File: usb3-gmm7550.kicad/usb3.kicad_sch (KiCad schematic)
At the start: 30 parts

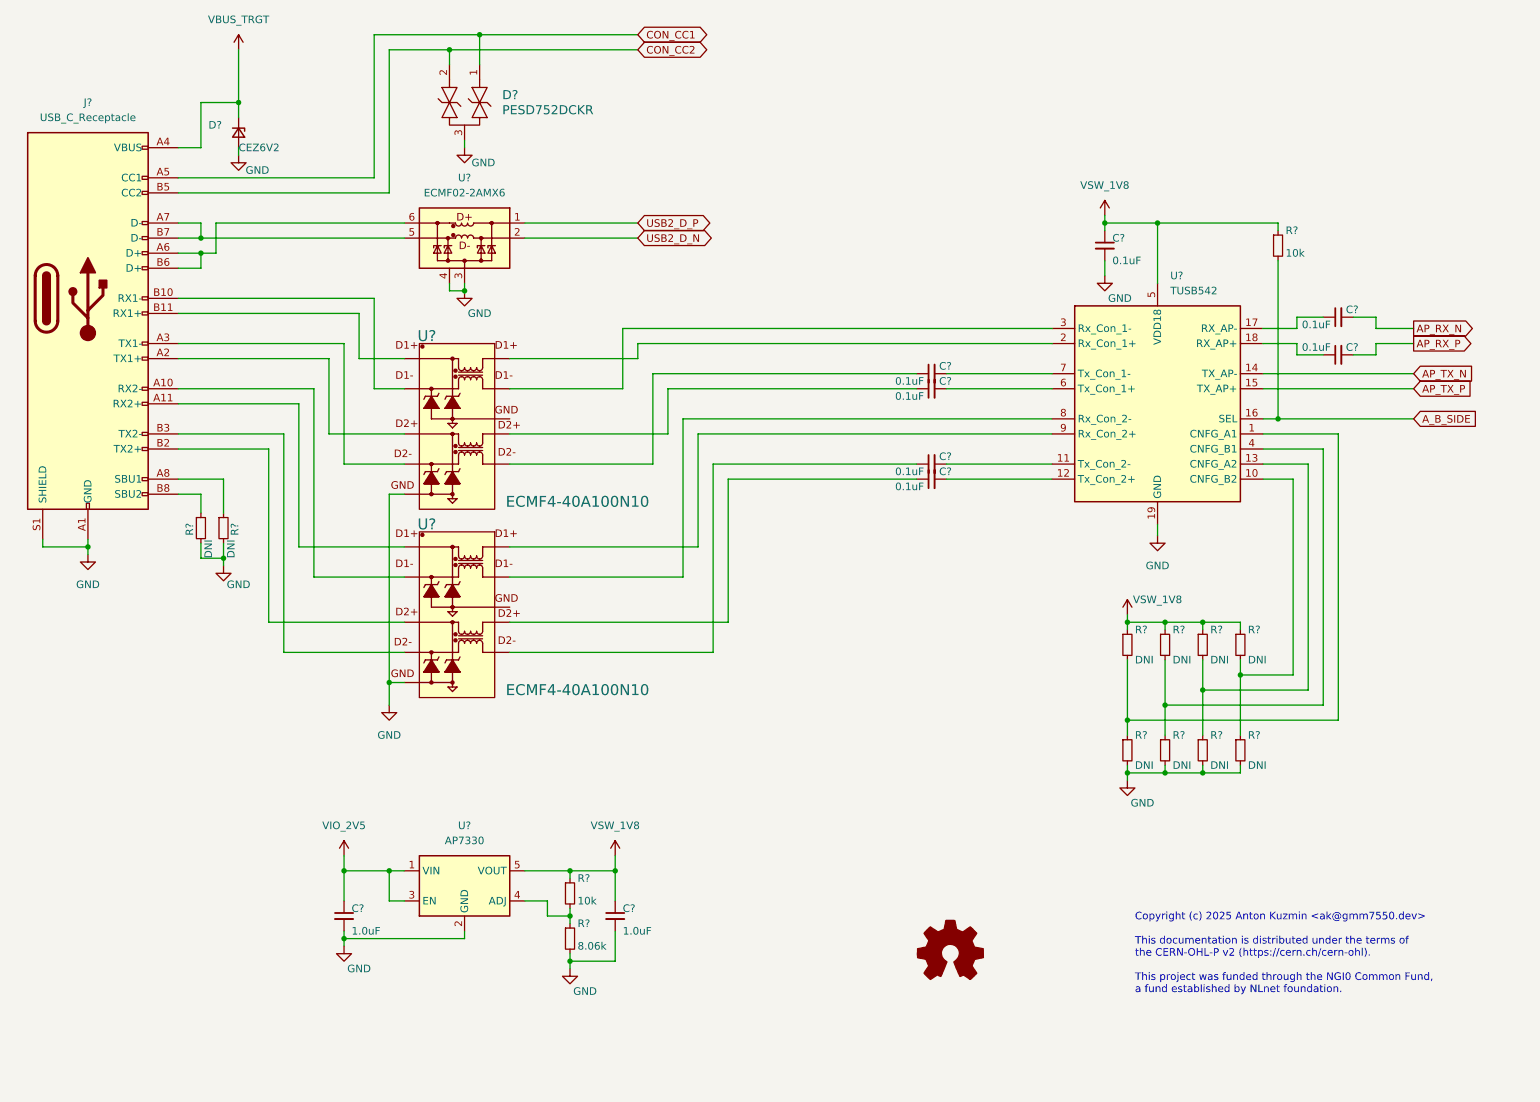
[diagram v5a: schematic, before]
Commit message: USB 3 adapter schematic: revision 0.9 (pre-layout) is ready
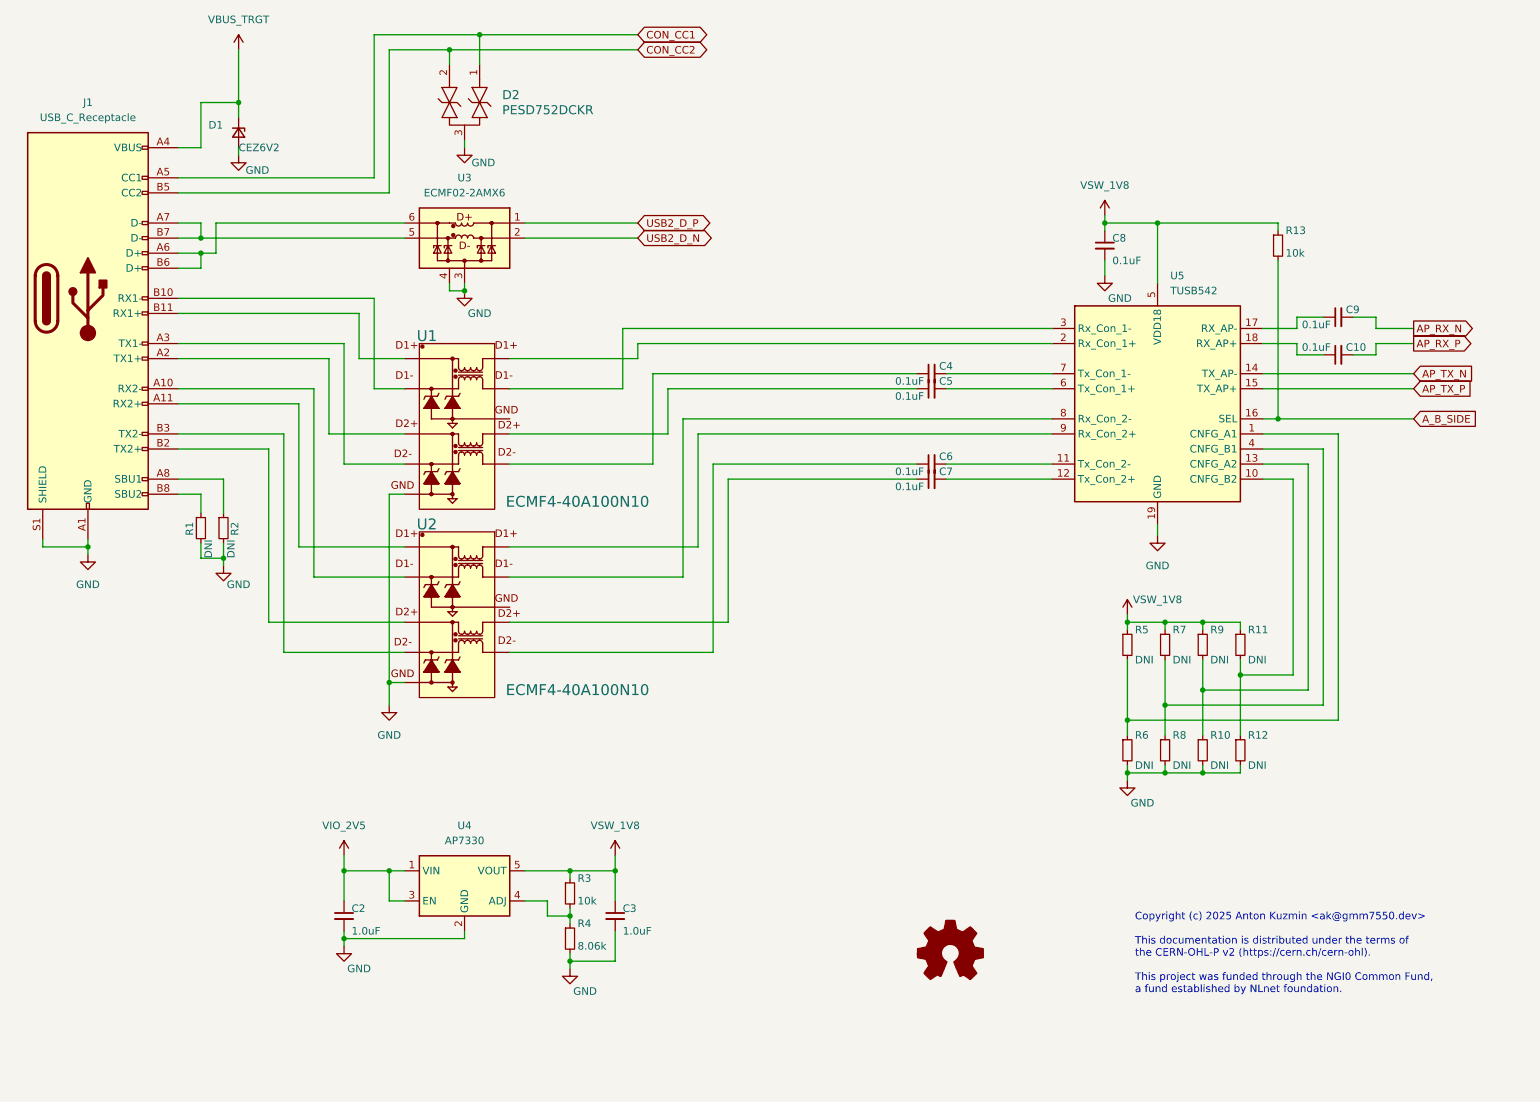
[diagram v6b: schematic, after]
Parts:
- gave numbers to parts that had none: 30

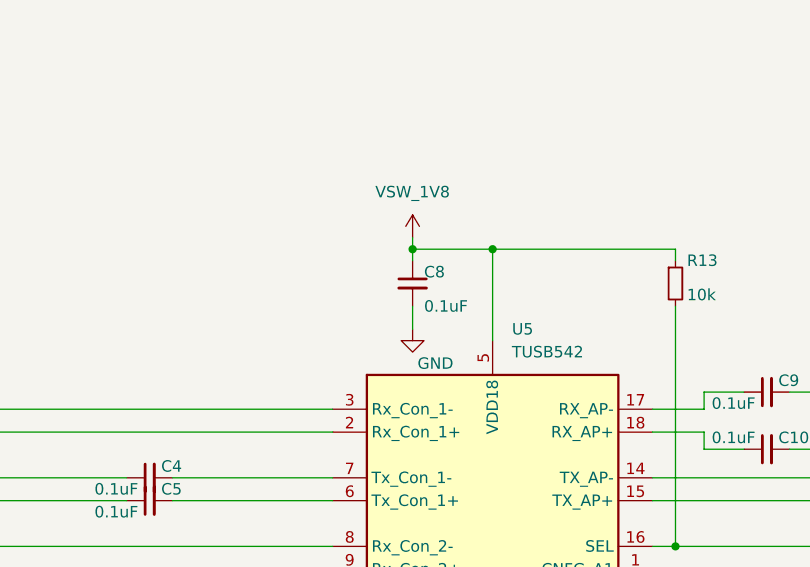
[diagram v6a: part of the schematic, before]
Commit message: Placement: WIP, schematic update to 0.9.1 -- BoM simplification and minor improvements
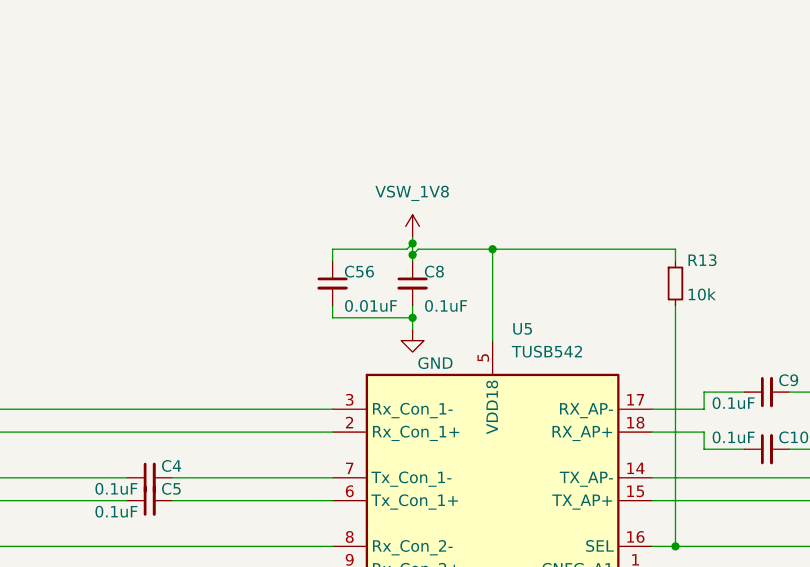
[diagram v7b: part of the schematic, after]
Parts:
- added C56: 0.01uF, Capacitor_SMD:C_0402_1005Metric, symbol Device:C_Small
- D2: footprint SOT-SC70_DCK_TEX -> usb3-gmm7550:SOT-SC70_DCK_TEX
- J1: footprint (none) -> Connector_USB:USB_C_Receptacle_Molex_105450-0101
- U1, U2: footprint ST_QFN40P220X135X50-10L -> usb3-gmm7550:UQFN10L_1P4X2P25X0P4_STM
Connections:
- net GND: now also C56.2
- net VSW_1V8: now also C56.1
